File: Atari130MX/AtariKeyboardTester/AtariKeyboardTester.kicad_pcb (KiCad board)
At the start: 2 copper layers, 129.5 x 125.1 mm, 213 parts

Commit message: Keyboard tester finalized
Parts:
- removed D_Fn_1, D_Fn_2, D_Fn_3, D_Fn_4, D_Help_1, D_LED_1, D_Option_1, D_Reset_1, D_Select_1, D_Start_1: LED, LED_THT:LED_D3.0mm
- added F1: LED, LED_THT:LED_D3.0mm, F.Cu at (71.0, 112.8)
- added F2: LED, LED_THT:LED_D3.0mm, F.Cu at (76.0, 112.8)
- added F3: LED, LED_THT:LED_D3.0mm, F.Cu at (81.1, 112.8)
- added F4: LED, LED_THT:LED_D3.0mm, F.Cu at (86.2, 112.8)
- added Help: LED, LED_THT:LED_D3.0mm, F.Cu at (93.8, 112.8)
- added Option: LED, LED_THT:LED_D3.0mm, F.Cu at (109.1, 112.8)
- added POWER LED: LED, LED_THT:LED_D3.0mm, F.Cu at (43.0, 112.8)
- added Reset: LED, LED_THT:LED_D3.0mm, F.Cu at (114.1, 112.8)
- added Select: LED, LED_THT:LED_D3.0mm, F.Cu at (104.0, 112.8)
- added Start: LED, LED_THT:LED_D3.0mm, F.Cu at (98.9, 112.8)
- * ^ →: renamed from D_*_1
- + \ ←: renamed from D_+_1
- 0 ): renamed from D_0_1
- 1 !: renamed from D_1_1
- 2 ": renamed from D_2_1
- 3 #: renamed from D_3_1
- 4 $: renamed from D_4_1
- 5 %: renamed from D_5_1
- 6 &: renamed from D_6_1
- 7 ': renamed from D_7_1
- 8 @: renamed from D_8_1
- 9 (: renamed from D_9_1
- ; :: renamed from D_;_1
- < Clr: renamed from D_<_1
- = | ↓: renamed from D_=_1
- > Ins: renamed from D_>_1
- Del BkSp: renamed from D_Del_1
- _ - ↑: renamed from D_-_1
- renumbered D_B_2 to 1, D_B_11 to 10, R_LED_COL_14 to 100, R_LED_COL_5 to 100, R_LED_COL_4 to 100, R_LED_COL_3 to 100, R_LED_COL_2 to 100, R_LED_COL_1 to 100, R24 to 100, R23 to 100, R22 to 100, R21 to 100, R20 to 100, R_LED_COL_13 to 100, R19 to 100, R18 to 100, R17 to 100, R16 to 100, R15 to 100, R14 to 100, R13 to 100, R12 to 100, R11 to 100, R10 to 100, R_LED_COL_12 to 100, R9 to 100, R8 to 100, R7 to 100, R6 to 100, R5 to 100, R4 to 100, R_LED_COL_11 to 100, R_LED_COL_10 to 100, R_LED_COL_9 to 100, R_LED_COL_8 to 100, R_LED_COL_7 to 100, R_LED_COL_6 to 100, D_B_12 to 11, D_B_13 to 12, D_B_14 to 13, D_B_15 to 14, D_B_16 to 15, D_B_17 to 16, D_B_18 to 17, D_B_19 to 18, D_B_20 to 19, D_B_3 to 2, D_B_21 to 20, D_B_22 to 21, D_B_23 to 22, D_B_24 to 23, D_B_25 to 24, D_B_4 to 3, D_B_5 to 4, D_B_6 to 5, D_B_7 to 6, D_B_8 to 7, D_B_9 to 8, D_B_10 to 9, D_A_1 to A, D_Break_1 to Break, D_Control_1 to Control, D_D_1 to D, D_E_1 to E, D_Esc_1 to Esc, D_F_1 to F, D_G_1 to G, D_H_1 to H, D_I_1 to I, D_J_1 to J, D_K_1 to K, D_L_1 to L, D_O_1 to O, D_P_1 to P, D_Q_1 to Q, D_R_1 to R, D_Return_1 to Return, D_S_1 to S, D_T_1 to T, D_Tab_1 to Tab, D_U_1 to U, D_W_1 to W, D_Y_1 to Y
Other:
- board text added: "(c) Bertrand Le Roy 2021 https://github.com/bleroy/3d-junkyard/tree/main/Atari130MX https://atariage.com/forums/profile/76850-screamingattheradio/ https://www.twitch.tv/screamingattheradio https://www.youtube.com/channel/UCyaCK4oVWf1ty618W-MJcrg"
- board text added: "Columns"
- board text added: "KeebTester XL/XE Rev. A"
- board text added: "Rows"

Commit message: Adjustments to Rev. D
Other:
- board text added: "NPN"
- board text added: "PNP"

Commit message: Atari keyboard tester Rev. B
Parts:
- added SW1: SW_SPST, Button_Switch_THT:SW_E-Switch_EG1224_SPDT_Angled, F.Cu at (143.8, 38.5)
- *: renamed from * ^ →; footprint LED_THT:LED_D3.0mm -> AtariKeyboardTester:LED_D3.0mm
- +: renamed from + \ ←; footprint LED_THT:LED_D3.0mm -> AtariKeyboardTester:LED_D3.0mm
- ,: renamed from , [; footprint LED_THT:LED_D3.0mm -> AtariKeyboardTester:LED_D3.0mm
- -: renamed from _ - ↑; footprint LED_THT:LED_D3.0mm -> AtariKeyboardTester:LED_D3.0mm
- .: renamed from . ]; footprint LED_THT:LED_D3.0mm -> AtariKeyboardTester:LED_D3.0mm
- /: renamed from / ?; footprint LED_THT:LED_D3.0mm -> AtariKeyboardTester:LED_D3.0mm
- 0: renamed from 0 ); footprint LED_THT:LED_D3.0mm -> AtariKeyboardTester:LED_D3.0mm
- 1, 10, 11, 12, 13, 14, 15, 16, 17, 18, 19, 2, 20, 21, 22, 23, 24, 3, 4, 5, 6, 7, 8, 9, A, B, Break, C, Caps, Control, D, D_A_10, D_A_11, D_A_12, D_A_13, D_A_14, D_A_15, D_A_16, D_A_17, D_A_18, D_A_19, D_A_2, D_A_20, D_A_21, D_A_22, D_A_23, D_A_24, D_A_25, D_A_3, D_A_4, D_A_5, D_A_6, D_A_7, D_A_8, D_A_9, E, Esc, F, F1, F2, F3, F4, G, H, Help, I, Inv, J, K, L, M, N, O, Option, P, Q, R, Reset, Return, S, Select, Shift (x2), Start, T, Tab, U, V, W, X, Y, Z: footprint LED_THT:LED_D3.0mm -> AtariKeyboardTester:LED_D3.0mm
- 1: renamed from 1 !; footprint LED_THT:LED_D3.0mm -> AtariKeyboardTester:LED_D3.0mm
- 2: renamed from 2 "; footprint LED_THT:LED_D3.0mm -> AtariKeyboardTester:LED_D3.0mm
- 3: renamed from 3 #; footprint LED_THT:LED_D3.0mm -> AtariKeyboardTester:LED_D3.0mm
- 4: renamed from 4 $; footprint LED_THT:LED_D3.0mm -> AtariKeyboardTester:LED_D3.0mm
- 5: renamed from 5 %; footprint LED_THT:LED_D3.0mm -> AtariKeyboardTester:LED_D3.0mm
- 6: renamed from 6 &; footprint LED_THT:LED_D3.0mm -> AtariKeyboardTester:LED_D3.0mm
- 7: renamed from 7 '; footprint LED_THT:LED_D3.0mm -> AtariKeyboardTester:LED_D3.0mm
- 8: renamed from 8 @; footprint LED_THT:LED_D3.0mm -> AtariKeyboardTester:LED_D3.0mm
- 9: renamed from 9 (; footprint LED_THT:LED_D3.0mm -> AtariKeyboardTester:LED_D3.0mm
- ;: renamed from ; :; footprint LED_THT:LED_D3.0mm -> AtariKeyboardTester:LED_D3.0mm
- <: renamed from < Clr; footprint LED_THT:LED_D3.0mm -> AtariKeyboardTester:LED_D3.0mm
- =: renamed from = | ↓; footprint LED_THT:LED_D3.0mm -> AtariKeyboardTester:LED_D3.0mm
- >: renamed from > Ins; footprint LED_THT:LED_D3.0mm -> AtariKeyboardTester:LED_D3.0mm
- BT1: renamed from 2x AAA; footprint Battery:BatteryHolder_Keystone_2468_2xAAA -> Battery:BatteryHolder_MPD_BA9VPC_1xPP3
- Del: renamed from Del BkSp; footprint LED_THT:LED_D3.0mm -> AtariKeyboardTester:LED_D3.0mm
- J1: renamed from Atari Connector
- J2: renamed from Pin headers
- J4: renamed from FFC 1-25 3-26
- JP1: renamed from XL/XE configuration
- Power LED: renamed from POWER LED; footprint LED_THT:LED_D3.0mm -> AtariKeyboardTester:LED_D3.0mm
- R1, R2, R3: value 100 -> 300
- REF** (x4): value MountingHole_2.2mm_M2 -> MountingHole_2.7mm_Pad; footprint MountingHole:MountingHole_2.2mm_M2 -> MountingHole:MountingHole_2.7mm_Pad
- Spaaace!: renamed from Space; footprint LED_THT:LED_D3.0mm -> AtariKeyboardTester:LED_D3.0mm
- moved REF** 3.97 mm to (135.1, 27.7)
- moved BT1 1.62 mm to (147.0, 82.6)
- renumbered 100 to 300, IDC to J3
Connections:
- BT1 pad 1: VCC -> Net-(BT1-Pad1)
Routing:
- net Net-(BT1-Pad1): track 0.00 -> 50.4 mm
- net VCC: track 127.4 -> 161.4 mm, vias 0 -> 2
- net ROW_2: track 230.2 -> 204.1 mm, vias 4 -> 2
- net ROW_9: track 294.6 -> 279.0 mm
- net ROW_8: track 167.1 -> 162.5 mm
- net GND: track 5.28 -> 3.02 mm, vias 78 -> 100
- net ROW_6: track 177.5 -> 175.9 mm
- net ROW_4: track 145.4 -> 144.5 mm
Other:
- board text added: "KeebTester XL/XE Rev. B"
- board text removed: "KeebTester XL/XE Rev. A"

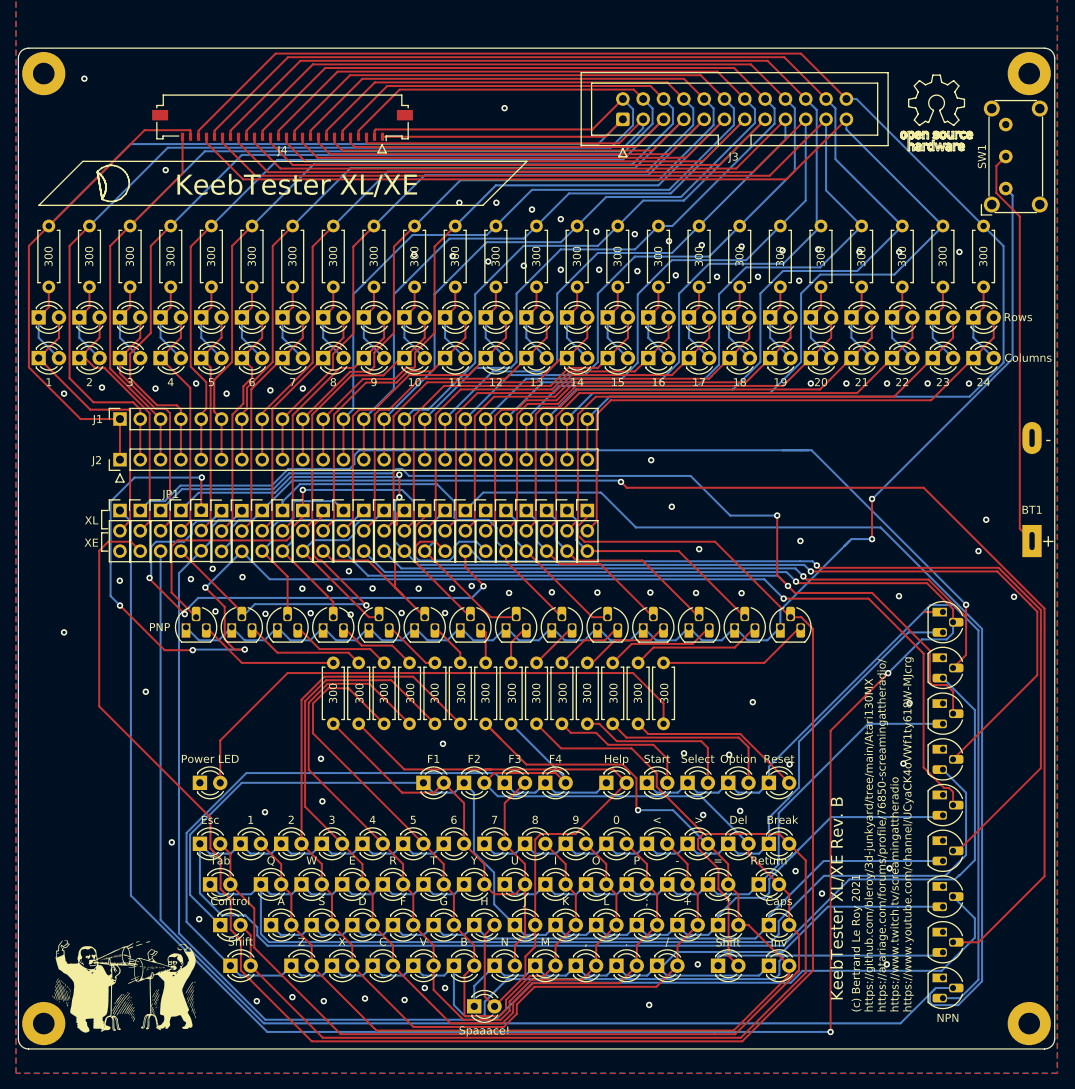
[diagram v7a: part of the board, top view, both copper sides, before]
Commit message: Minor keyboard tester updates
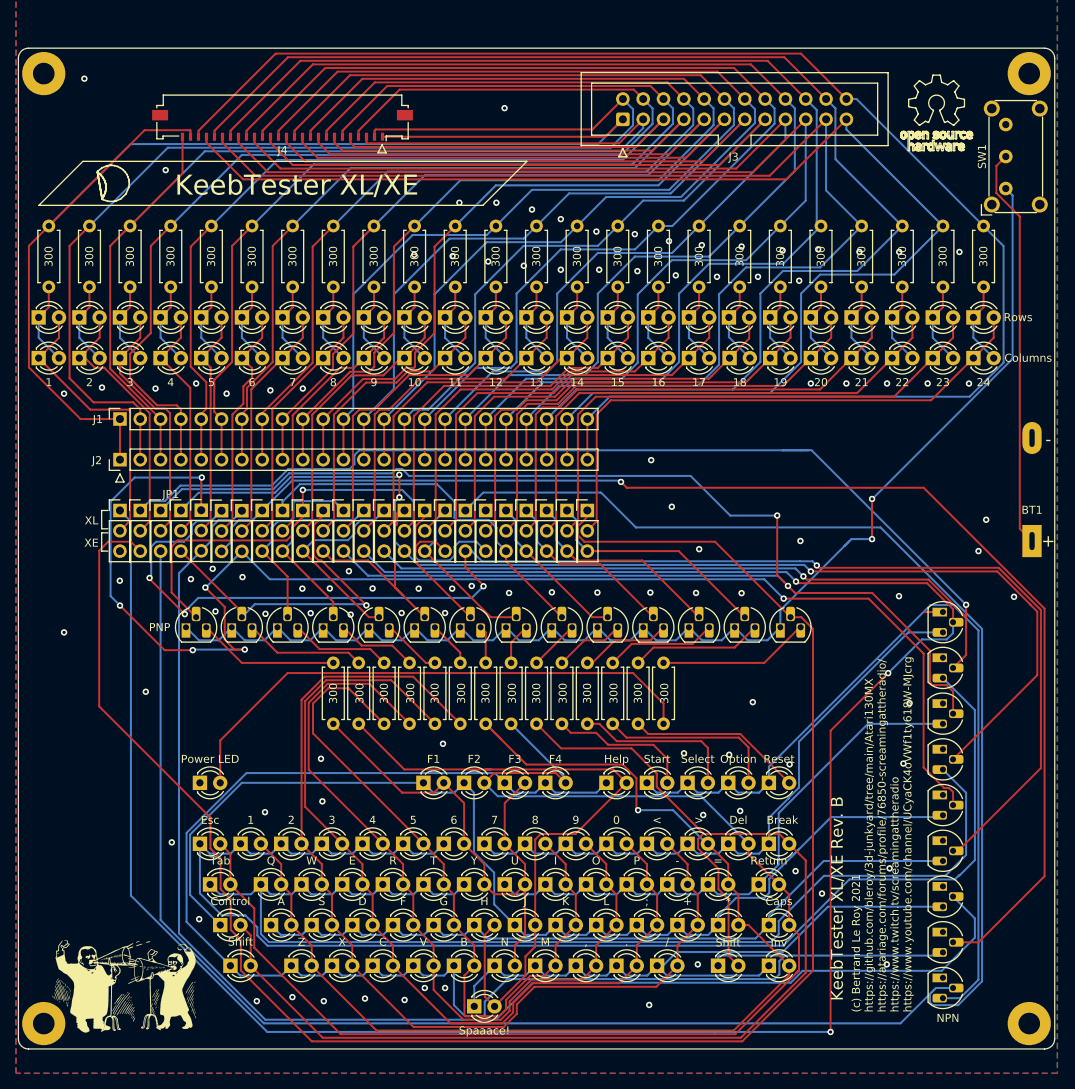
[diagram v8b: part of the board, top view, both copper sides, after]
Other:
- net class Default removed
